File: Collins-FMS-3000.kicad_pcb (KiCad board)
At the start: 2 copper layers, 145 x 160 mm, 192 parts, among them J1 USB_B_Mini, J2 AVR-ISP-6, J3 Conn_01x04, SW70 SW_Push, U1 ATmega32U4-MU, U2 MCP23017_SO, U3 MCP23017_SO, U4 IS31FL3733B, Y1 16MHz

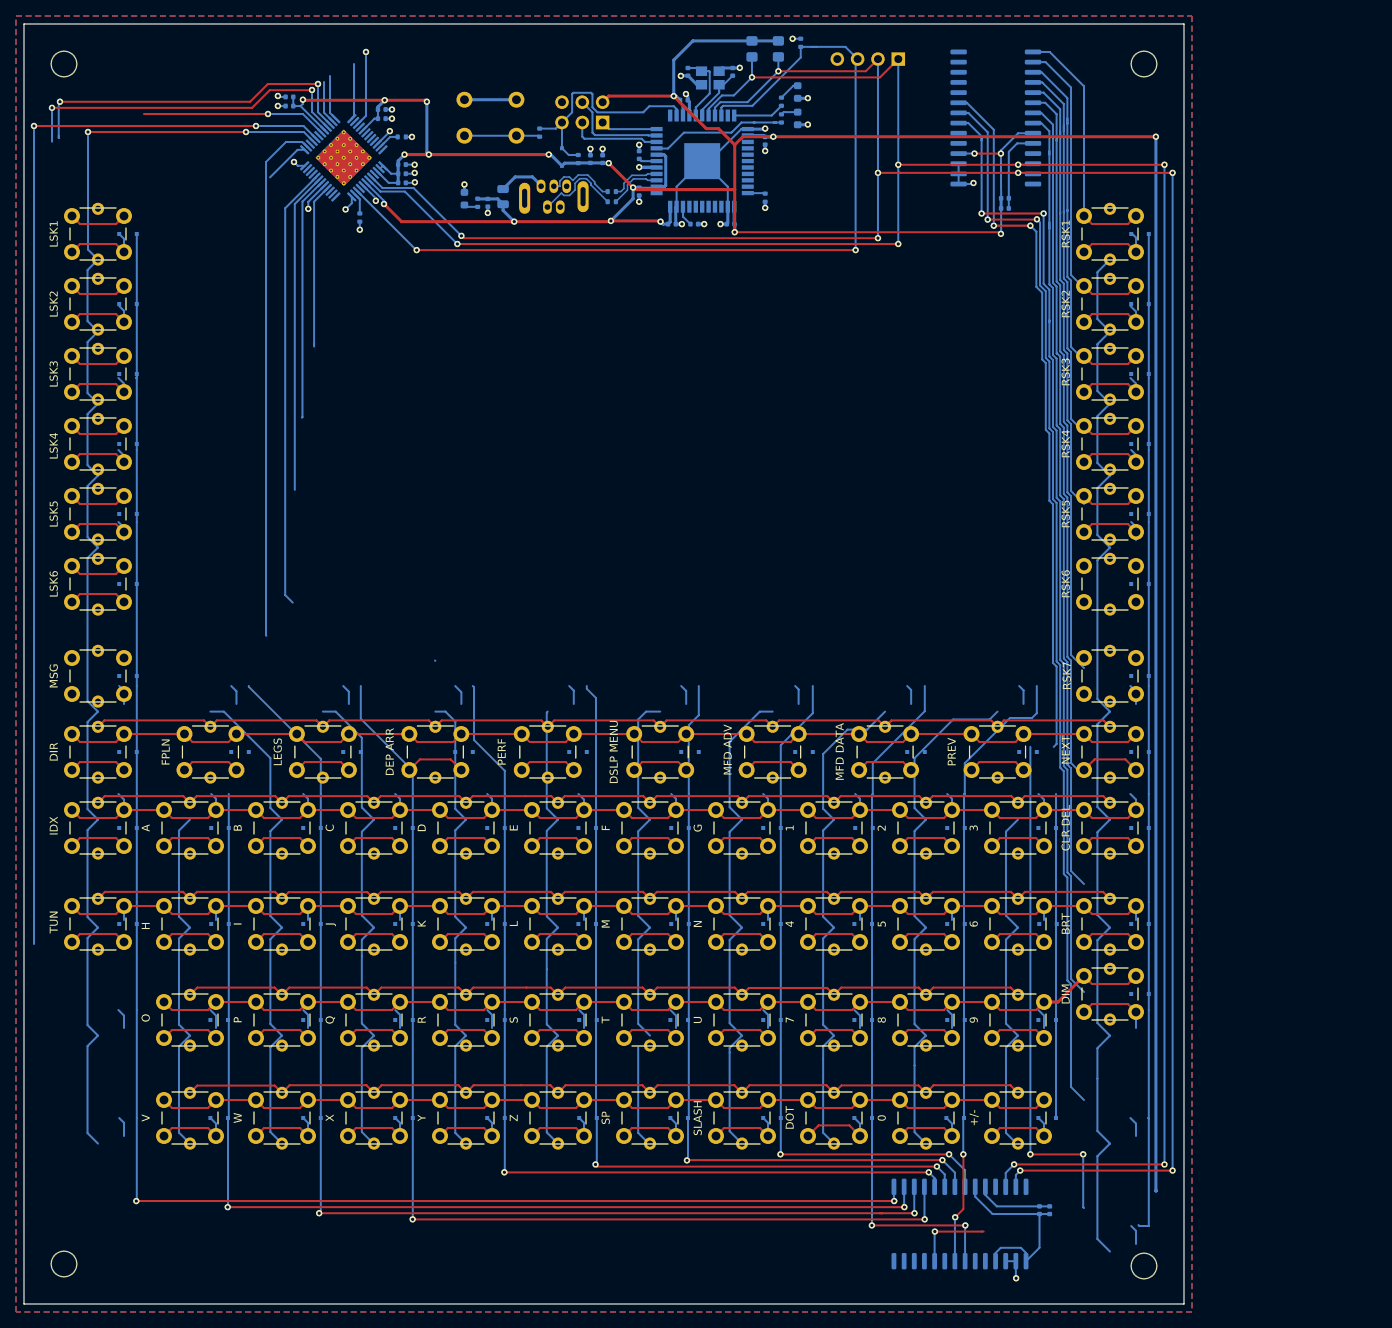
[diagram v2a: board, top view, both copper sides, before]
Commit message: Round edges, clean up traces, add placement marks
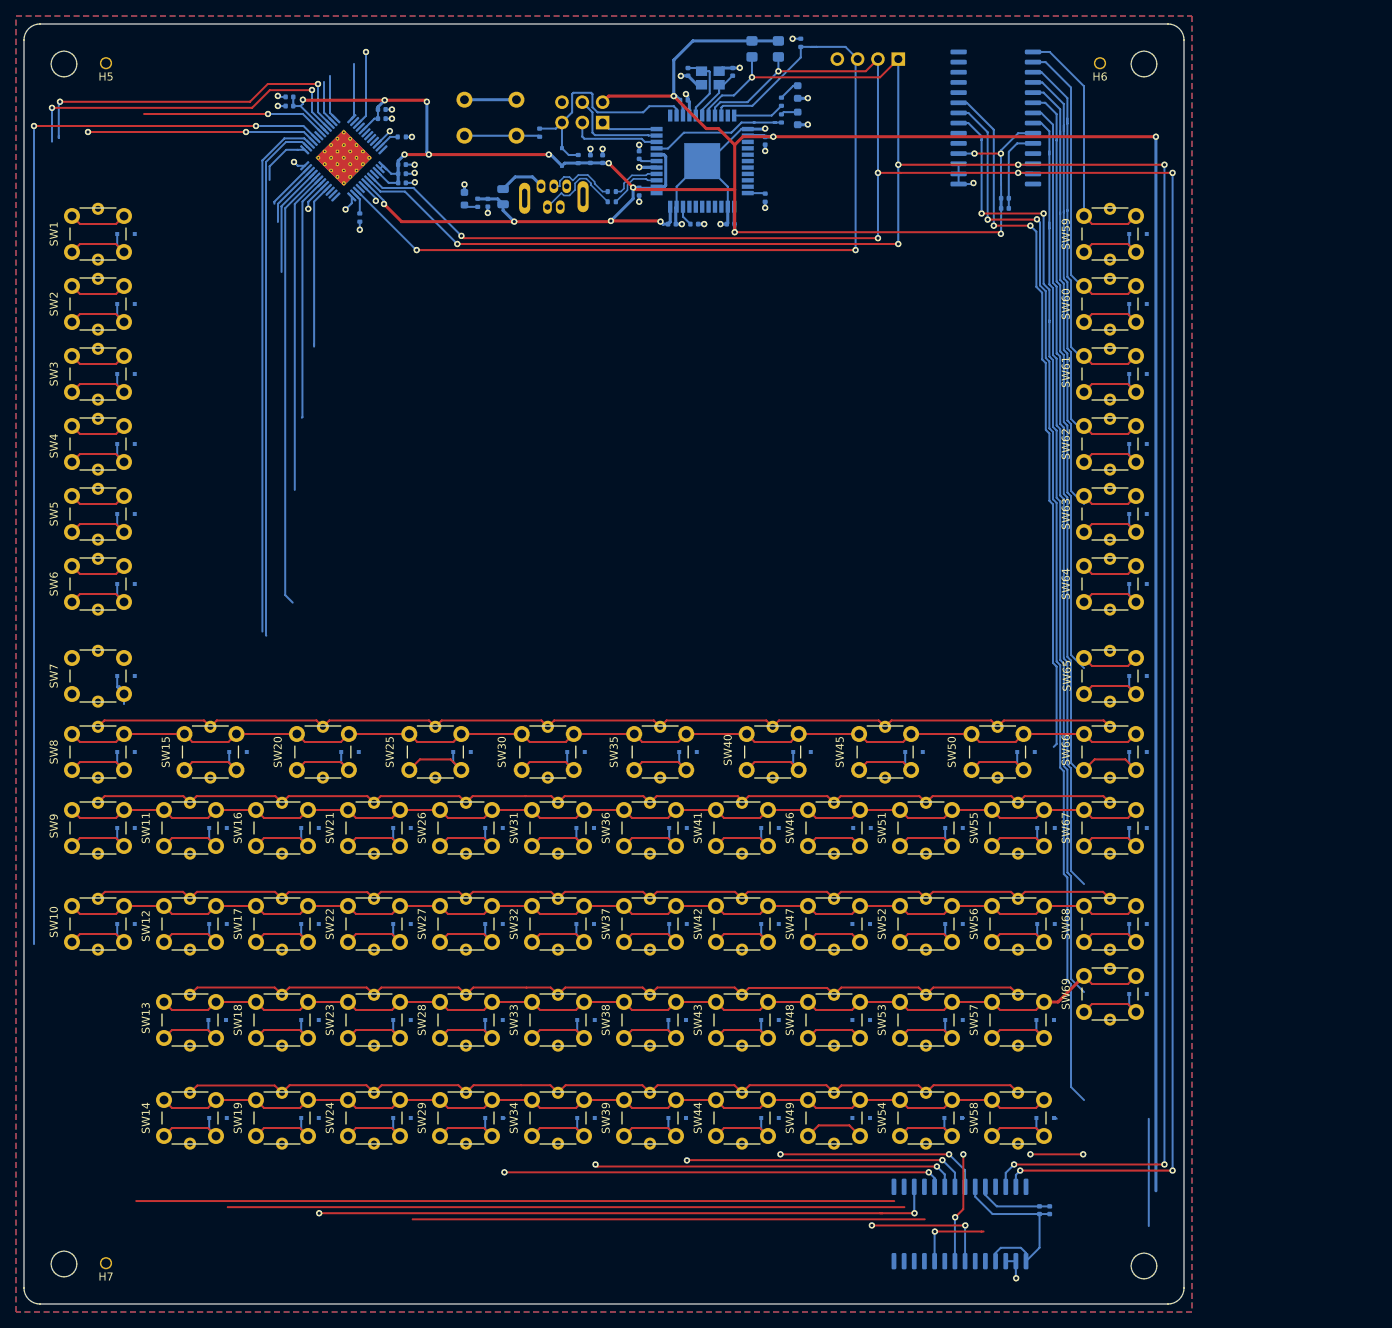
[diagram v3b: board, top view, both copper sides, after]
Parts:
- added H5: MountingHole, Collins-FMS-3000:JLCPCB_Tooling_Hole, F.Cu at (30.2, 25.0)
- added H6: MountingHole, Collins-FMS-3000:JLCPCB_Tooling_Hole, F.Cu at (154.5, 25.0)
- added H7: MountingHole, Collins-FMS-3000:JLCPCB_Tooling_Hole, F.Cu at (30.2, 175.0)
- SW25: renamed from DEP ARR
- SW35: renamed from DSLP MENU
- SW40: renamed from MFD ADV
- SW45: renamed from MFD DATA
- SW67: renamed from CLR DEL
- moved D1 0.25 mm to (32.8, 46.2)
- moved D10 0.25 mm to (32.8, 132.5)
- moved D11 0.25 mm to (44.2, 120.5)
- moved D12 0.25 mm to (44.2, 132.5)
- moved D13 0.25 mm to (44.1, 144.5)
- moved D15 0.25 mm to (46.8, 111.0)
- moved D16 0.25 mm to (55.8, 120.5)
- moved D17 0.25 mm to (55.8, 132.5)
- moved D18 0.25 mm to (55.8, 144.5)
- moved D19 0.25 mm to (55.8, 156.8)
- moved D2 0.25 mm to (32.8, 55.0)
- moved D20 0.25 mm to (60.8, 111.0)
- moved D21 0.25 mm to (67.2, 120.5)
- moved D22 0.25 mm to (67.2, 132.5)
- moved D23 0.25 mm to (67.2, 144.5)
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- renumbered LSK1 to SW1, TUN to SW10, A to SW11, H to SW12, O to SW13, V to SW14, FPLN to SW15, B to SW16, I to SW17, P to SW18, W to SW19, LSK2 to SW2, LEGS to SW20, C to SW21, J to SW22, Q to SW23, X to SW24, D to SW26, K to SW27, R to SW28, Y to SW29, LSK3 to SW3, PERF to SW30, E to SW31, L to SW32, S to SW33, Z to SW34, F to SW36, M to SW37, T to SW38, SP to SW39, LSK4 to SW4, G to SW41, N to SW42, U to SW43, SLASH to SW44, 1 to SW46, 4 to SW47, 7 to SW48, DOT to SW49, LSK5 to SW5, PREV to SW50, 2 to SW51, 5 to SW52, 8 to SW53, 0 to SW54, 3 to SW55, 6 to SW56, 9 to SW57, +/- to SW58, RSK1 to SW59, LSK6 to SW6, RSK2 to SW60, RSK3 to SW61, RSK4 to SW62, RSK5 to SW63, RSK6 to SW64, RSK7 to SW65, NEXT to SW66, BRT to SW68, DIM to SW69, MSG to SW7, DIR to SW8, IDX to SW9
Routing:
- net /LEDMatrix/CS12: track 137.0 -> 0.00 mm
- net /LEDMatrix/CS1: track 165.4 -> 28.6 mm
- net /ButtonMatrix/COL0: track 217.6 -> 94.7 mm, vias 2 -> 0
- net /ButtonMatrix/COL11: track 135.2 -> 23.2 mm
- net /ButtonMatrix/COL3: track 137.5 -> 64.0 mm, vias 2 -> 0
- net /ButtonMatrix/COL8: track 86.3 -> 16.2 mm
- net /ButtonMatrix/COL2: track 147.7 -> 78.3 mm
- net /LEDMatrix/SW12: track 110.7 -> 177.0 mm
- net /LEDMatrix/CS10: track 65.1 -> 0.00 mm
- net /ButtonMatrix/COL9: track 77.8 -> 13.9 mm
- net /LEDMatrix/CS9: track 69.5 -> 6.95 mm
- net /ButtonMatrix/COL4: track 117.8 -> 55.4 mm
- net /LEDMatrix/CS3: track 62.3 -> 0.00 mm
- net /LEDMatrix/CS8: track 67.3 -> 5.64 mm
- net /LEDMatrix/CS4: track 84.7 -> 23.2 mm
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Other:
- outline, holes or cut-outs redrawn
- board text added: "JLCJLCJLCJLC"

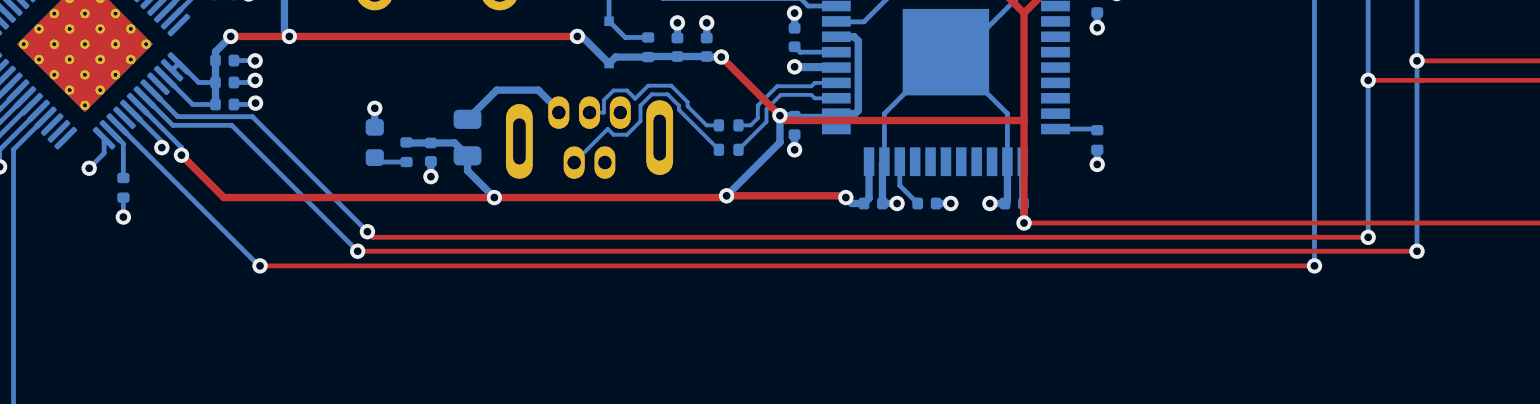
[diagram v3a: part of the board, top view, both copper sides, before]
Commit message: Add INTB connection
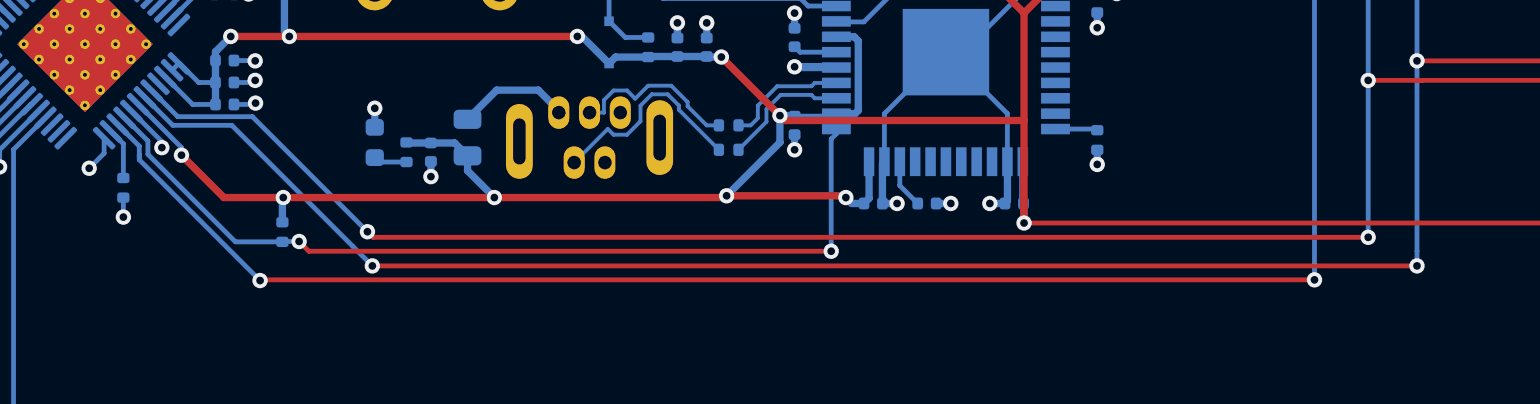
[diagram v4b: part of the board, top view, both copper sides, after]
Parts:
- added R4: 100k, Resistor_SMD:R_0402_1005Metric, B.Cu at (70.2, 46.5)
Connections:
- U1 pad 1: Net-(U1-Pad1) -> INTB
- U4 pad 45: Net-(U4-Pad45) -> INTB
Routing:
- net INTB: track 0.00 -> 46.5 mm, vias 0 -> 2
- net SDB: track 112.6 -> 114.2 mm
- net +5V: track 478.4 -> 479.7 mm, vias 19 -> 20
- net I2C_SCL: track 304.5 -> 305.5 mm
